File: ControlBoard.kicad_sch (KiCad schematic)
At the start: 0 parts

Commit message: 增加部分接口
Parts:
- added J1, J2: Conn_02x06_Odd_Even, symbol Connector_Generic:Conn_02x06_Odd_Even
- added J3: Conn_02x03_Odd_Even, symbol Connector_Generic:Conn_02x03_Odd_Even
- added J4: Conn_01x02, symbol Connector_Generic:Conn_01x02
- added P1: USB_C_Plug_USB2.0, symbol Connector:USB_C_Plug_USB2.0
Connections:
- new net: P1.A1 (GND), P1.A12 (GND), P1.B1 (GND), P1.B12 (GND)
- new net: P1.A4 (VBUS), P1.A9 (VBUS), P1.B4 (VBUS), P1.B9 (VBUS)
- new net +3.3V: J2.9 (Pin_9), J3.1 (Pin_1)
- new net +5V: J2.7 (Pin_7)
- new net ADC1_BusCurr: J1.9 (Pin_9)
- new net ADC1_BusVol: J1.7 (Pin_7)
- new net ADC1_U: J1.1 (Pin_1)
- new net ADC1_V: J1.3 (Pin_3)
- new net ADC1_W: J1.5 (Pin_5)
- new net ADC2_U: J2.1 (Pin_1)
- new net ADC2_V: J2.3 (Pin_3)
- new net ADC2_W: J2.5 (Pin_5)
- new net CAN_H: J4.2 (Pin_2)
- new net CAN_L: J4.1 (Pin_1)
- new net Debug_Rx: J3.6 (Pin_6)
- new net Debug_Tx: J3.5 (Pin_5)
- new net Debug_sck: J3.3 (Pin_3)
- new net Debug_swd: J3.4 (Pin_4)
- new net GND: J1.11 (Pin_11), J2.11 (Pin_11), J3.2 (Pin_2)
- new net PWM1_CH1: J1.2 (Pin_2)
- new net PWM1_CH1N: J1.4 (Pin_4)
- new net PWM1_CH2: J1.6 (Pin_6)
- new net PWM1_CH2N: J1.8 (Pin_8)
- new net PWM1_CH3: J1.10 (Pin_10)
- new net PWM1_CH3N: J1.12 (Pin_12)
- new net PWM8_CH1: J2.2 (Pin_2)
- new net PWM8_CH1N: J2.4 (Pin_4)
- new net PWM8_CH2: J2.6 (Pin_6)
- new net PWM8_CH2N: J2.8 (Pin_8)
- new net PWM8_CH3: J2.10 (Pin_10)
- new net PWM8_CH3N: J2.12 (Pin_12)
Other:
- added sheet MCU_Part (MCU_Part.kicad_sch)

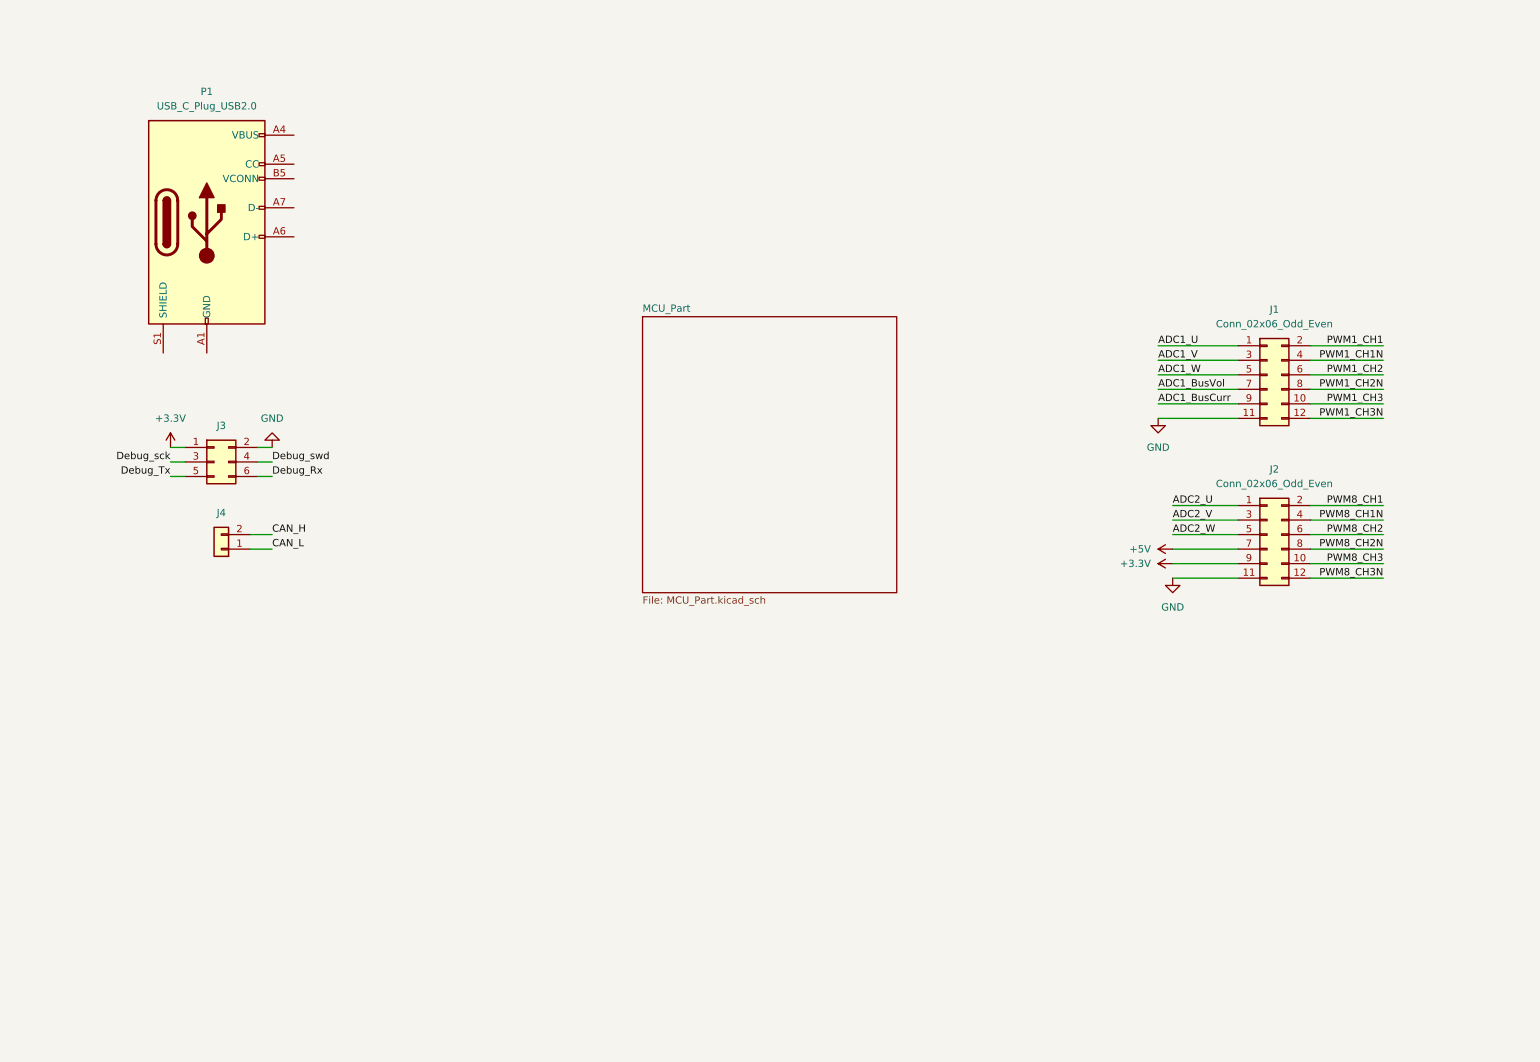
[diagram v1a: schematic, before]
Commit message: 增加PWM/SPI部分接口
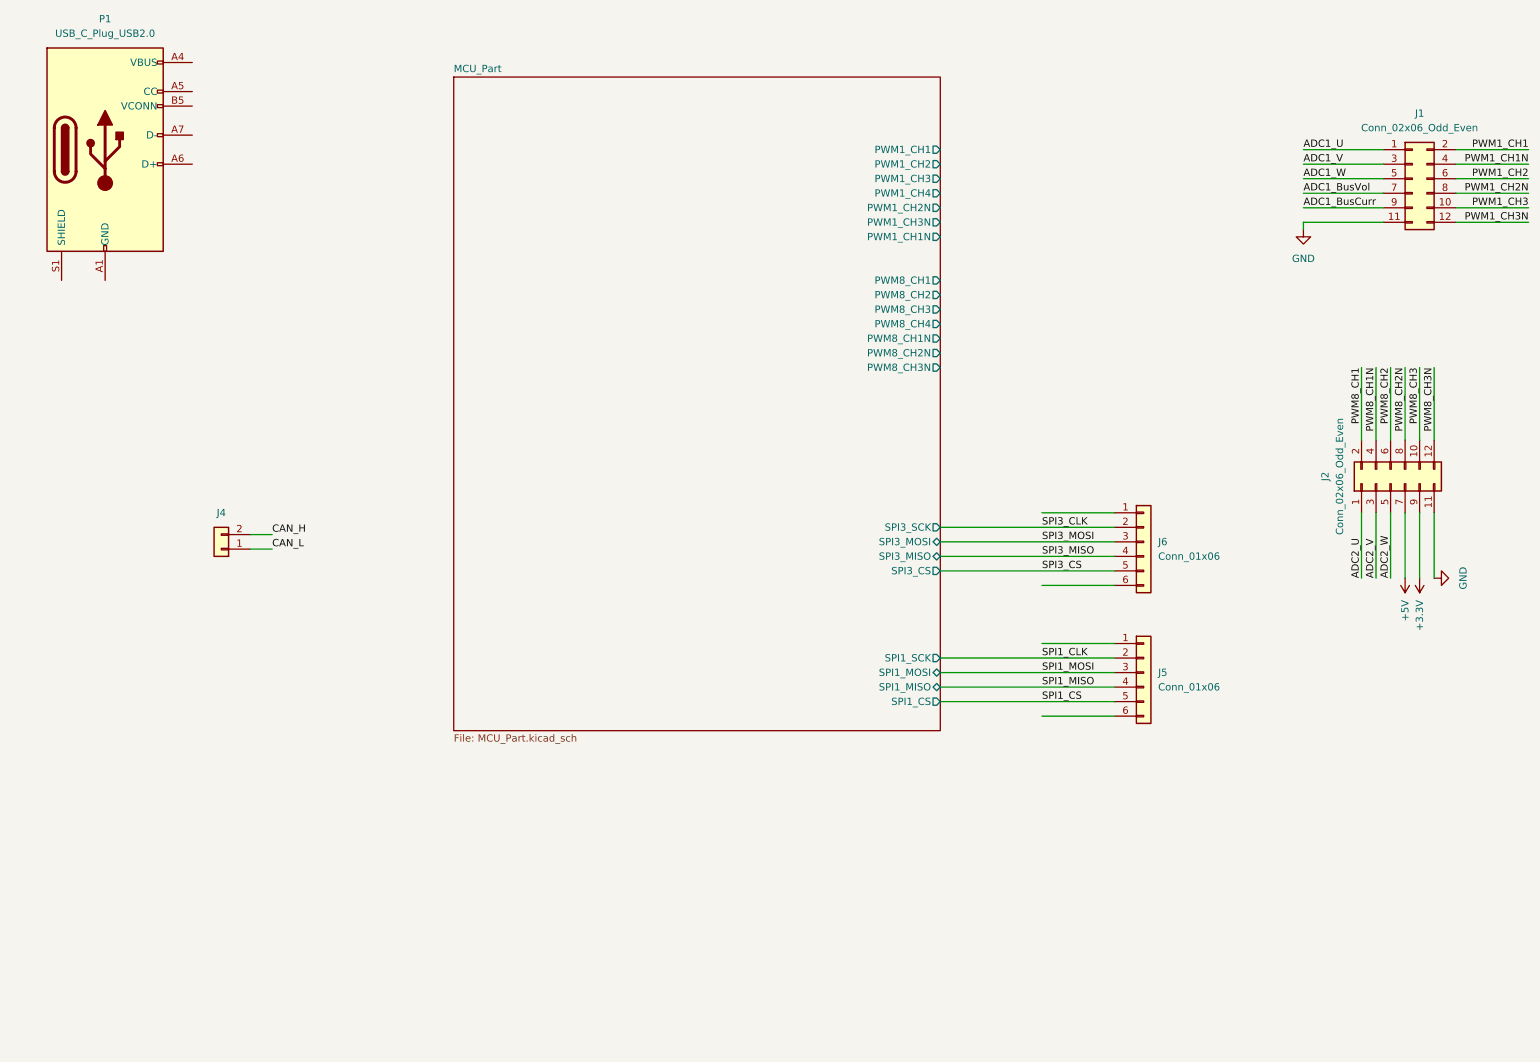
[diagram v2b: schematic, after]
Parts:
- removed J3: Conn_02x03_Odd_Even, symbol Connector_Generic:Conn_02x03_Odd_Even
- added J5, J6: Conn_01x06, symbol Connector_Generic:Conn_01x06
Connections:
- new net SPI1_CLK: J5.2 (Pin_2)
- new net SPI1_CS: J5.5 (Pin_5)
- new net SPI1_MISO: J5.4 (Pin_4)
- new net SPI1_MOSI: J5.3 (Pin_3)
- new net SPI3_CLK: J6.2 (Pin_2)
- new net SPI3_CS: J6.5 (Pin_5)
- new net SPI3_MISO: J6.4 (Pin_4)
- new net SPI3_MOSI: J6.3 (Pin_3)
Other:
- sheet MCU_Part ports: added PWM1_CH1, PWM1_CH1N, PWM1_CH2, PWM1_CH2N, PWM1_CH3, PWM1_CH3N, PWM1_CH4, PWM8_CH1, PWM8_CH1N, PWM8_CH2, PWM8_CH2N, PWM8_CH3, PWM8_CH3N, PWM8_CH4, SPI1_CS, SPI1_MISO, SPI1_MOSI, SPI1_SCK, SPI3_CS, SPI3_MISO, SPI3_MOSI, SPI3_SCK; removed none
- moved on the sheet: J1, J2, P1

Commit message: 增加ADC采样，优化PWM
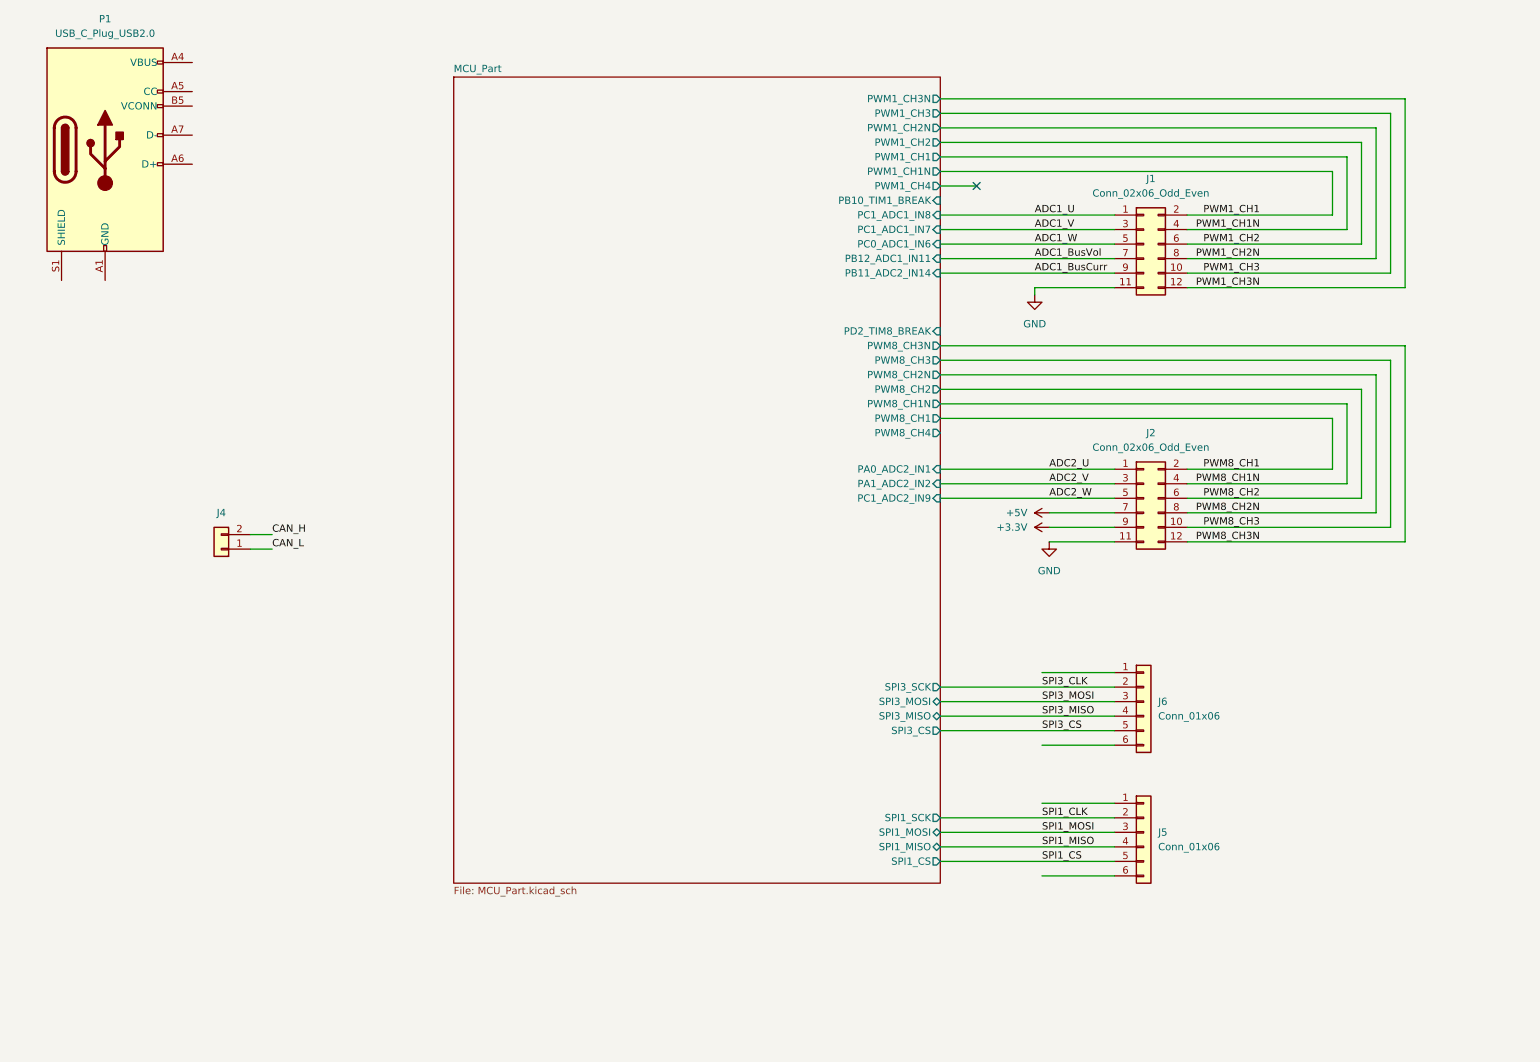
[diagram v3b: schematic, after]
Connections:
- no-connect marks 0 -> 1
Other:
- sheet MCU_Part ports: added PA0_ADC2_IN1, PA1_ADC2_IN2, PB10_TIM1_BREAK, PB11_ADC2_IN14, PB12_ADC1_IN11, PC0_ADC1_IN6, PC1_ADC1_IN7, PC1_ADC1_IN8, PC1_ADC2_IN9, PD2_TIM8_BREAK; removed none
- moved on the sheet: J1, J2, J5, J6

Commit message: 完成部分I2C/FDCAN引脚分配
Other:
- sheet MCU_Part ports: added PB0_ADC1_IN15, PB12_FDCAN2_RX, PB6_FDCAN2_TX; removed PB12_ADC1_IN11
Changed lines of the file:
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@@
-			)
-		)
-		(pin "PB12_ADC1_IN11" input
-			(at 173.99 57.15 0)
-			(effects
-				(font
-					(size 1.27 1.27)
-				)
-				(justify right)
 			)
 		)
@@
 			(effects
 				(font
+					(size 1.27 1.27)
+				)
+				(justify right)
+			)
+		)
+		(pin "PB12_FDCAN2_RX" bidirectional
+			(at 88.9 99.06 180)
+			(effects
+				(font
+					(size 1.27 1.27)
+				)
+				(justify left)
+			)
+		)
+		(pin "PB6_FDCAN2_TX" bidirectional
+			(at 88.9 96.52 180)
+			(effects
+				(font
+					(size 1.27 1.27)
+				)
+				(justify left)
+			)
+		)
+		(pin "PB0_ADC1_IN15" input
+			(at 173.99 57.15 0)
+			(effects
+				(font

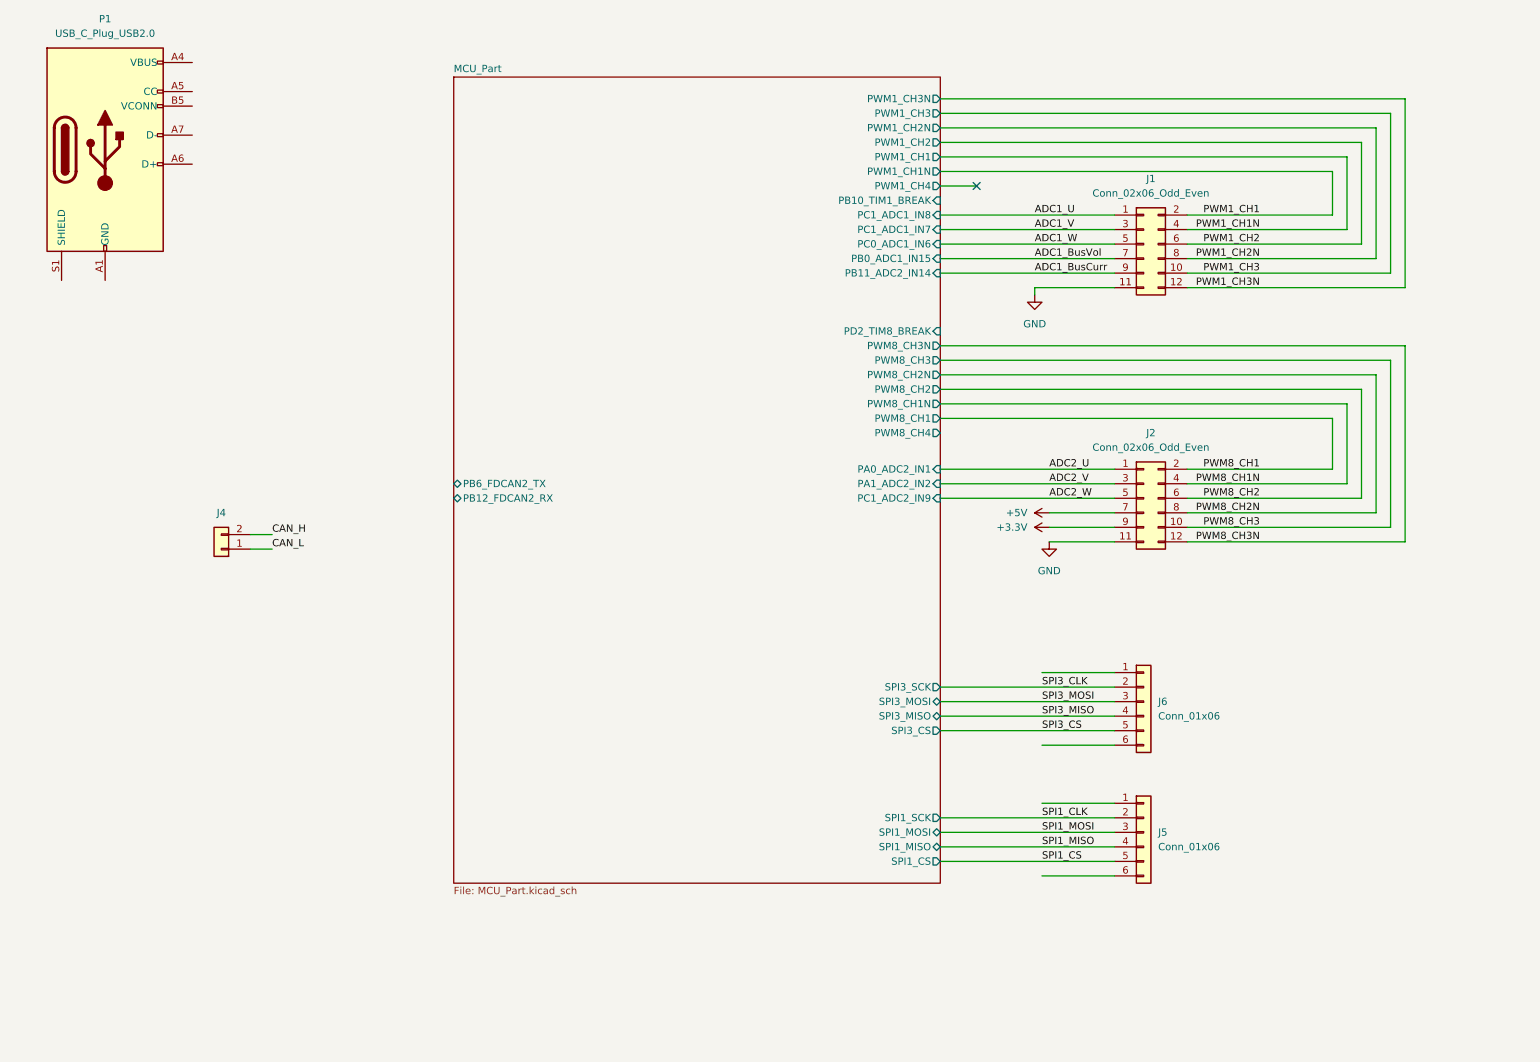
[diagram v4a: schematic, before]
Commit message: 增加3.3V电路
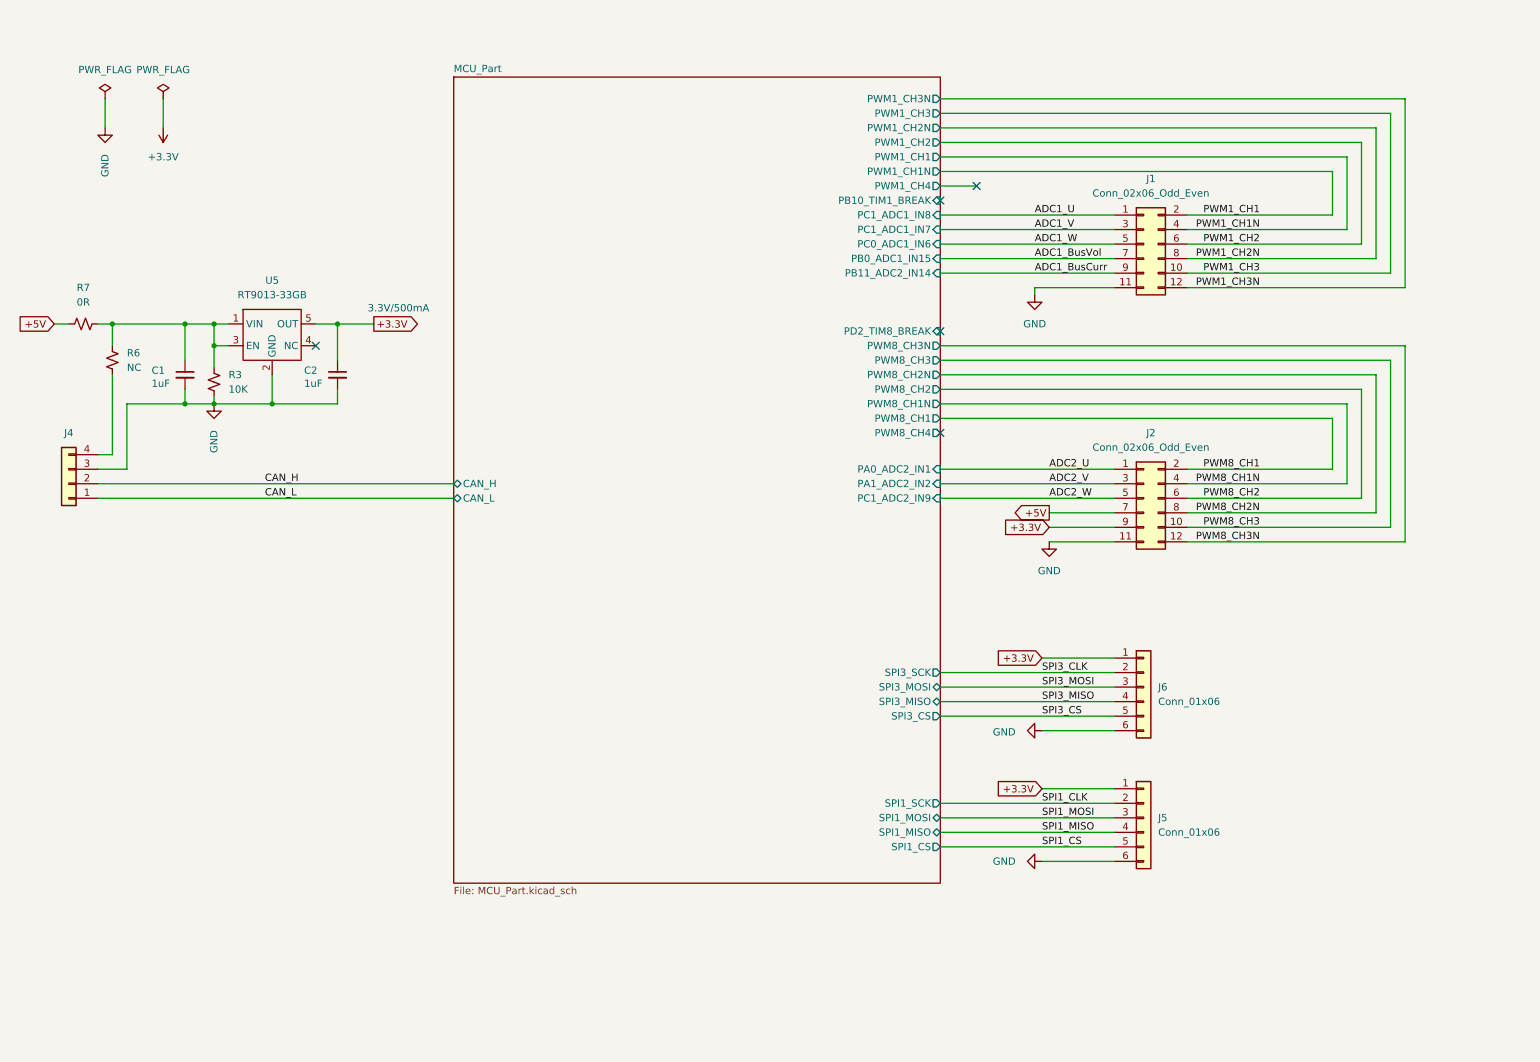
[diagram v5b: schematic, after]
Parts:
- removed J4: Conn_01x02, symbol Connector_Generic:Conn_01x02
- removed P1: USB_C_Plug_USB2.0, symbol Connector:USB_C_Plug_USB2.0
- added C1, C2: 1uF, symbol Device:C_Small
- added J4: Conn_01x04, symbol Connector_Generic:Conn_01x04
- added R3: 10K, symbol Device:R_Small_US
- added R6: NC, symbol Device:R_Small_US
- added R7: 0R, symbol Device:R_Small_US
- added U5: RT9013-33GB, symbol User_Driver:RT9013-33GB
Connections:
- net +3.3V: now also J5.1 (Pin_1), J6.1 (Pin_1), C2.1, U5.5 (OUT)
- net +5V: now also R7.1
- net CAN_H: now also J4.2 (Pin_2)
- net CAN_L: now also J4.1 (Pin_1)
- net GND: now also J5.6 (Pin_6), J6.6 (Pin_6), C1.2, C2.2, J4.3 (Pin_3), R3.2, U5.2 (GND)
- new net: C1.1, R3.1, R6.1, R7.2, U5.1 (VIN), U5.3 (EN)
- new net: J4.4 (Pin_4), R6.2
- no-connect marks 1 -> 5
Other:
- sheet MCU_Part ports: added CAN_H, CAN_L; removed PB12_FDCAN2_RX, PB6_FDCAN2_TX
- note added: "3.3V/500mA"
- moved on the sheet: J5, J6

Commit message: 优化EEPROM电路
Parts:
- removed C1, C2: 1uF, symbol Device:C_Small
- removed J4: Conn_01x04, symbol Connector_Generic:Conn_01x04
- removed R3: 10K, symbol Device:R_Small_US
- removed R6: NC, symbol Device:R_Small_US
- removed R7: 0R, symbol Device:R_Small_US
- removed U5: RT9013-33GB, symbol User_Driver:RT9013-33GB
- added J3: Conn_02x03_Odd_Even, symbol Connector_Generic:Conn_02x03_Odd_Even
- added J7: Conn_01x02, symbol Connector_Generic:Conn_01x02
- added R5: 0R, symbol Device:R_Small_US
- added TP1, TP2: TestPoint_Small, symbol Connector:TestPoint_Small
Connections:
- net +3.3V: no longer J2.9 (Pin_9), J5.1 (Pin_1), J6.1 (Pin_1)
- net CAN_H: now also J7.2 (Pin_2)
- net CAN_L: now also J7.1 (Pin_1)
- net GND: now also J3.2 (Pin_2)
- net MCU_Part/PWM1_CH4: now also TP1.1
- net MCU_Part/PWM8_CH4: now also TP2.1
- new net: J3.1 (Pin_1), R5.2
- new net 3.3V: J2.9 (Pin_9), J5.1 (Pin_1), J6.1 (Pin_1), R5.1
- new net Debug_Rx: J3.6 (Pin_6)
- new net Debug_Tx: J3.4 (Pin_4)
- new net Debug_sck: J3.5 (Pin_5)
- new net Debug_swd: J3.3 (Pin_3)
- no-connect marks 5 -> 2
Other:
- added sheet Power (Power.kicad_sch)
- sheet MCU_Part ports: added PA13_SWD_SDO, PA14_SWD_SCK, PC4_UART1_RX, PC5_UART1_TX; removed none
- note removed: "3.3V/500mA"
